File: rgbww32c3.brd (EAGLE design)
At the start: 36.8 x 20.3 mm, 19 parts, among them IC2 7805TV

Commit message: adjusted channel names
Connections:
- net CH1: now also SV1.8, U$1.5, U$1.6; no longer SV1.4, U$3.5, U$3.6
- net CH2: now also SV1.7, U$1.7, U$1.8; no longer SV1.5, U$2.7, U$2.8
- net CH4: now also SV1.5, U$2.7, U$2.8; no longer SV1.7, U$1.7, U$1.8
- net CH5: now also SV1.4, U$3.5, U$3.6; no longer SV1.8, U$1.5, U$1.6
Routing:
- net CH5: track 6.55 -> 8.59 mm
- net CH1: track 8.59 -> 6.55 mm
- net RX: track 23.8 -> 25.3 mm
- net CH4: track 7.08 -> 7.61 mm
- net CH2: track 7.61 -> 7.08 mm
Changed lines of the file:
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@@
 <text x="31.115" y="76.2" size="0.6096" layer="25">12V</text>
 <text x="31.115" y="73.66" size="0.6096" layer="25">12V</text>
-<text x="31.115" y="71.12" size="0.6096" layer="25">CH1</text>
-<text x="31.115" y="68.58" size="0.6096" layer="25">CH2</text>
+<text x="31.115" y="60.96" size="0.6096" layer="25">CH1</text>
+<text x="31.115" y="63.5" size="0.6096" layer="25">CH2</text>
 <text x="31.115" y="66.04" size="0.6096" layer="25">CH3</text>
-<text x="31.115" y="63.5" size="0.6096" layer="25">CH4</text>
-<text x="31.115" y="60.96" size="0.6096" layer="25">CH5</text>
+<text x="31.115" y="68.58" size="0.6096" layer="25">CH4</text>
+<text x="31.115" y="71.12" size="0.6096" layer="25">CH5</text>
 <wire x1="0.01" y1="80.01" x2="36.83" y2="80.01" width="0" layer="20"/>
 <text x="15.5575" y="64.92875" size="0.6096" layer="26" rot="MR90">G0</text>
@@
 </signal>
 <signal name="CH1">
-<contactref element="U$3" pad="5"/>
-<contactref element="U$3" pad="6"/>
-<contactref element="SV1" pad="4"/>
-<wire x1="34.29" y1="71.12" x2="33.02" y2="71.12" width="1.016" layer="1"/>
-<wire x1="33.02" y1="71.12" x2="29.21" y2="74.93" width="1.016" layer="1"/>
-<wire x1="29.21" y1="74.93" x2="29.21" y2="74.355" width="1.016" layer="1"/>
-<wire x1="29.21" y1="74.355" x2="29.27" y2="74.295" width="1.016" layer="1"/>
-<wire x1="29.27" y1="74.295" x2="29.27" y2="75.565" width="1.016" layer="1"/>
+<contactref element="U$1" pad="5"/>
+<contactref element="U$1" pad="6"/>
+<contactref element="SV1" pad="8"/>
+<wire x1="34.29" y1="60.96" x2="29.905" y2="60.96" width="1.016" layer="1"/>
+<wire x1="29.905" y1="60.96" x2="29.27" y2="61.595" width="1.016" layer="1"/>
+<wire x1="29.27" y1="61.595" x2="29.27" y2="62.865" width="1.016" layer="1"/>
 </signal>
 <signal name="CH3">
@@
 </signal>
 <signal name="CH2">
-<contactref element="U$2" pad="7"/>
-<contactref element="U$2" pad="8"/>
-<contactref element="SV1" pad="5"/>
-<wire x1="34.29" y1="68.58" x2="33.02" y2="68.58" width="1.016" layer="1"/>
-<wire x1="33.02" y1="68.58" x2="30.48" y2="71.12" width="1.016" layer="1"/>
-<wire x1="30.48" y1="71.12" x2="29.905" y2="71.12" width="1.016" layer="1"/>
-<wire x1="29.905" y1="71.12" x2="29.27" y2="70.485" width="1.016" layer="1"/>
-<wire x1="29.27" y1="70.485" x2="29.27" y2="71.755" width="1.016" layer="1"/>
-</signal>
-<signal name="CH4">
 <contactref element="U$1" pad="7"/>
 <contactref element="U$1" pad="8"/>
@@
 <wire x1="8.255" y1="72.54875" x2="8.09625" y2="72.39" width="0.3048" layer="1"/>
 <wire x1="8.09625" y1="72.39" x2="7.46125" y2="72.39" width="0.3048" layer="1"/>
-</signal>
-<signal name="CH5">
-<contactref element="U$1" pad="5"/>
-<contactref element="U$1" pad="6"/>
-<contactref element="SV1" pad="8"/>
-<wire x1="34.29" y1="60.96" x2="29.905" y2="60.96" width="1.016" layer="1"/>
-<wire x1="29.905" y1="60.96" x2="29.27" y2="61.595" width="1.016" layer="1"/>
-<wire x1="29.27" y1="61.595" x2="29.27" y2="62.865" width="1.016" layer="1"/>
 </signal>
 <signal name="12V">
@@
 <wire x1="13.17625" y1="72.39" x2="16.51" y2="72.39" width="0.3048" layer="1"/>
 <wire x1="16.51" y1="72.39" x2="17.145" y2="71.755" width="0.3048" layer="1"/>
-<wire x1="16.51" y1="72.39" x2="15.71625" y2="71.78875" width="0" layer="19" extent="1-16"/>
+<wire x1="15.71625" y1="71.78875" x2="17.145" y2="71.78875" width="0.3048" layer="16"/>
+<wire x1="17.145" y1="71.78875" x2="17.145" y2="71.755" width="0.3048" layer="16"/>
 </signal>
 <signal name="GPIO0">
@@
 <wire x1="16.1925" y1="68.705" x2="15.71625" y2="68.22875" width="0.3048" layer="16"/>
 </signal>
+<signal name="CH5">
+<contactref element="U$3" pad="5"/>
+<contactref element="U$3" pad="6"/>
+<contactref element="SV1" pad="4"/>
+<wire x1="34.29" y1="71.12" x2="33.02" y2="71.12" width="1.016" layer="1"/>
+<wire x1="33.02" y1="71.12" x2="29.21" y2="74.93" width="1.016" layer="1"/>
+<wire x1="29.21" y1="74.93" x2="29.21" y2="74.355" width="1.016" layer="1"/>
+<wire x1="29.21" y1="74.355" x2="29.27" y2="74.295" width="1.016" layer="1"/>
+<wire x1="29.27" y1="74.295" x2="29.27" y2="75.565" width="1.016" layer="1"/>
+</signal>
+<signal name="CH4">
+<contactref element="U$2" pad="7"/>
+<contactref element="U$2" pad="8"/>
+<contactref element="SV1" pad="5"/>
+<wire x1="34.29" y1="68.58" x2="33.02" y2="68.58" width="1.016" layer="1"/>
+<wire x1="33.02" y1="68.58" x2="30.48" y2="71.12" width="1.016" layer="1"/>
+<wire x1="30.48" y1="71.12" x2="29.905" y2="71.12" width="1.016" layer="1"/>
+<wire x1="29.905" y1="71.12" x2="29.27" y2="70.485" width="1.016" layer="1"/>
+<wire x1="29.27" y1="70.485" x2="29.27" y2="71.755" width="1.016" layer="1"/>
+</signal>
 </signals>

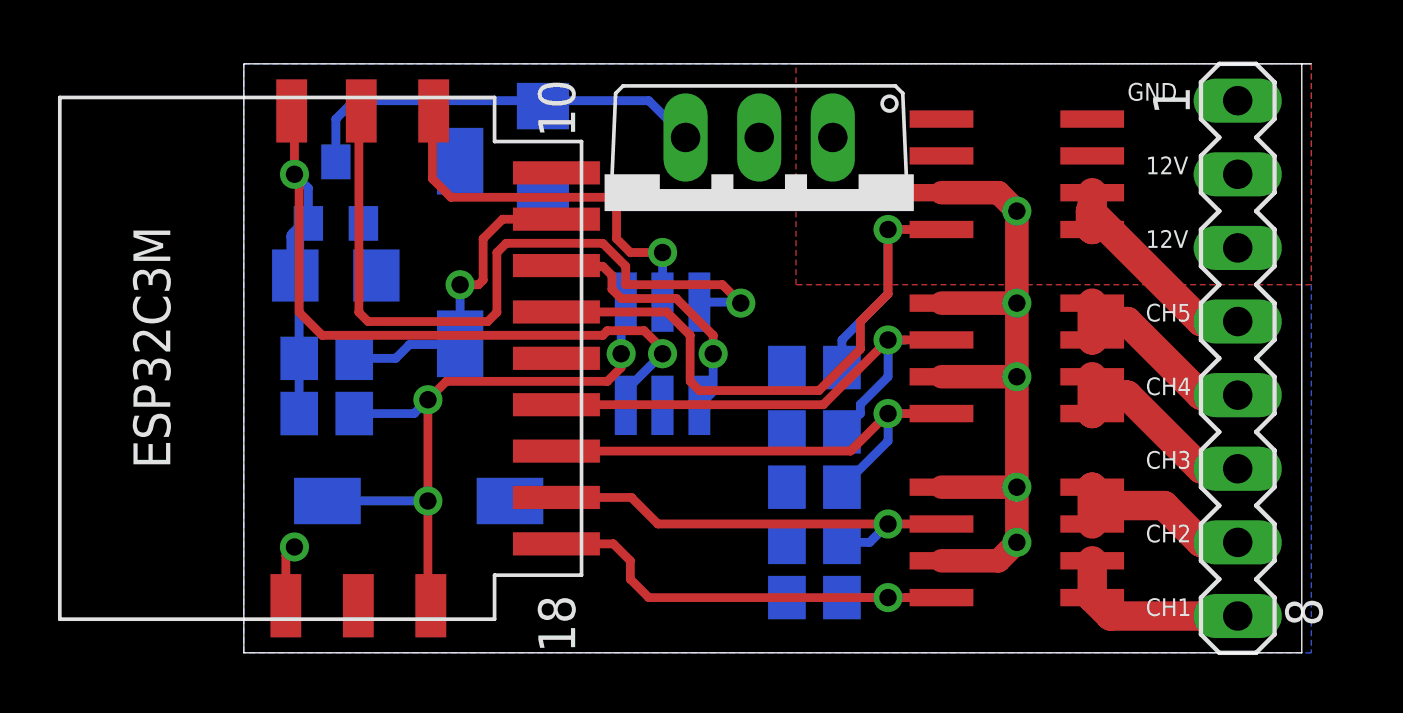
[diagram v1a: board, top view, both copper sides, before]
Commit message: initial testing version
programming the ESP32 now works using an esp_prog. It does require to pull GPIO9 low, hence the extra PRG button. The auto programming function of other ESP models (GPIO0) does not work on the C3, it seems.
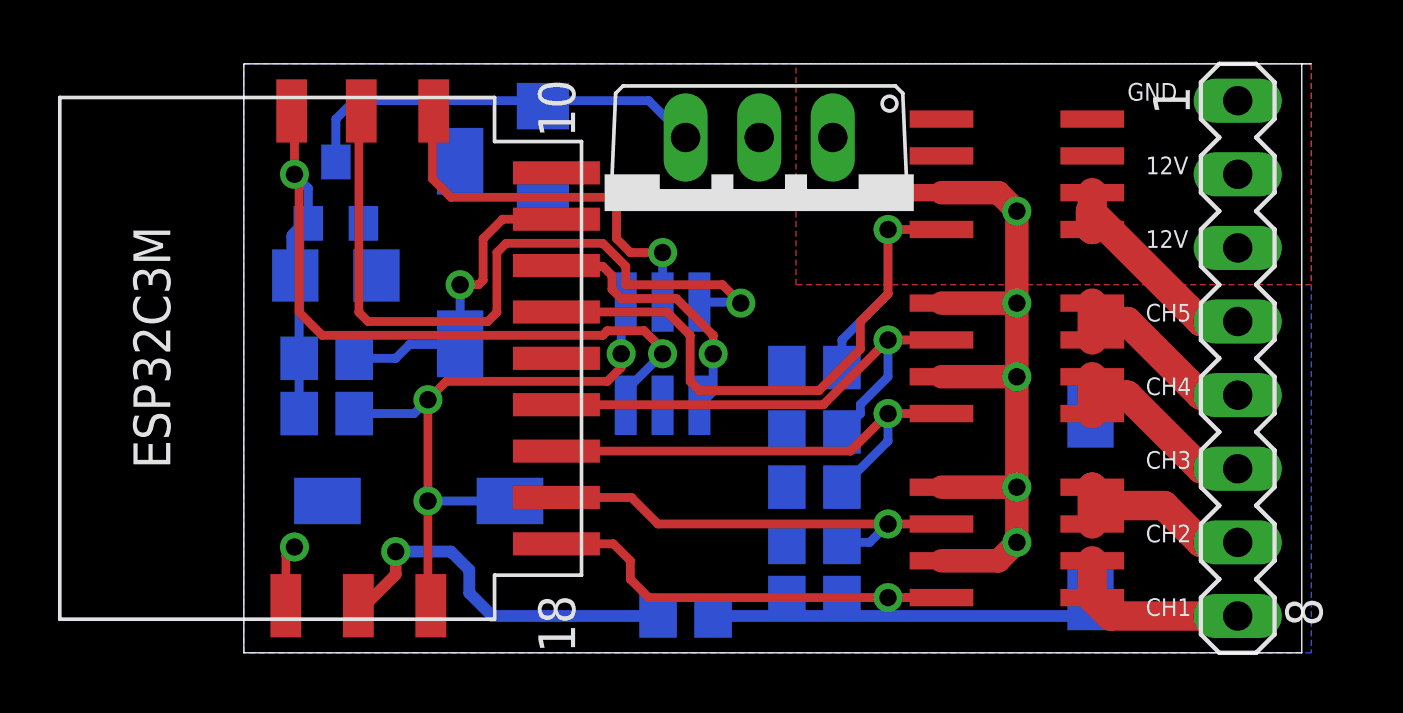
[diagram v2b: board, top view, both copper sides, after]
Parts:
- added J_PRG: 1296-T06, con-leotronics:06
- added R7: 10k, rcl:R0805
- PRG: value 1296-T06 -> (none); device con-leotronics:06 -> SparkFun-Electromechanical:TACTILE-SWITCH-1101NE
- moved PRG 15.7 mm to (29.2, 64.8), turned to 270 degrees
- turned RST to 180 degrees
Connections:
- new net N$1: R7.2, U$5.IO9
- new net N$2: PRG.2, R7.1
- net 3V3: now also J_PRG.2; no longer PRG.2
- net EN: now also J_PRG.1; no longer PRG.1
- net GND: now also J_PRG.4, PRG.1; no longer PRG.4
- net GPIO0: now also J_PRG.6; no longer PRG.6
- net RX: now also J_PRG.5; no longer PRG.5
- net TX: now also J_PRG.3; no longer PRG.3
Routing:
- net N$2: track 0.00 -> 13.3 mm
- net N$1: track 0.00 -> 13.0 mm, vias 0 -> 1
- net CH4: track 7.61 -> 6.71 mm
- net EN: track 23.0 -> 22.3 mm
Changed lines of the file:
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@@
 </element>
 <element name="R10" library="rcl" package="R0805" value="10k" x="2.8575" y="69.85" smashed="yes" rot="MR180"/>
-<element name="RST" library="SparkFun-Electromechanical" package="TACTILE-SWITCH-1101NE" value="" x="6.0325" y="64.92875" rot="MR0">
-<attribute name="PROD_ID" value="SWCH-00815" x="6.0325" y="71.27875" size="1.778" layer="28" rot="MR0" display="off"/>
+<element name="RST" library="SparkFun-Electromechanical" package="TACTILE-SWITCH-1101NE" value="" x="6.0325" y="64.92875" rot="MR180">
+<attribute name="PROD_ID" value="SWCH-00815" x="6.0325" y="58.57875" size="1.778" layer="28" rot="MR180" display="off"/>
 </element>
 <element name="R6" library="rcl" package="R0805" value="10k" x="2.8575" y="67.945" smashed="yes" rot="MR180">
 <attribute name="NAME" x="2.2225" y="66.675" size="1.27" layer="26" rot="MR180"/>
 </element>
-<element name="PRG" library="con-leotronics" package="06" value="1296-T06" x="14.44625" y="70.00875" smashed="yes" rot="MR180">
+<element name="J_PRG" library="con-leotronics" package="06" value="1296-T06" x="14.44625" y="70.00875" smashed="yes" rot="MR180">
 <attribute name="NAME" x="11.90625" y="71.27875" size="1.27" layer="26" rot="MR270"/>
 </element>
@@
 </element>
 <element name="C2" library="rcl" package="C1206" value="" x="10.31875" y="77.1525" rot="MR270"/>
+<element name="R7" library="rcl" package="R0805" value="10k" x="15.24" y="60.96" rot="MR0"/>
+<element name="PRG" library="SparkFun-Electromechanical" package="TACTILE-SWITCH-1101NE" value="" x="29.21" y="64.77" rot="MR270">
+<attribute name="PROD_ID" value="SWCH-00815" x="29.21" y="64.77" size="1.778" layer="28" rot="MR270" display="off"/>
+</element>
 </elements>
 <signals>
@@
 <contactref element="RST" pad="1"/>
 <contactref element="SV1" pad="1"/>
-<contactref element="PRG" pad="4"/>
+<contactref element="J_PRG" pad="4"/>
 <contactref element="C1" pad="2"/>
 <contactref element="C2" pad="2"/>
+<contactref element="PRG" pad="1"/>
 </signal>
 <signal name="CH1">
@@
 <contactref element="R6" pad="1"/>
 <contactref element="R10" pad="1"/>
-<contactref element="PRG" pad="2"/>
+<contactref element="J_PRG" pad="2"/>
 <contactref element="C1" pad="1"/>
 <wire x1="2.225" y1="74.505" x2="2.225" y2="75.72125" width="0.3048" layer="16"/>
@@
 <contactref element="U$5" pad="EN"/>
 <via x="6.35" y="64.92875" extent="1-16" drill="0.6"/>
-<contactref element="PRG" pad="1"/>
-<wire x1="2.8825" y1="64.92875" x2="6.35" y2="64.92875" width="0.3048" layer="16"/>
+<contactref element="J_PRG" pad="1"/>
+<wire x1="9.1825" y1="64.92875" x2="6.35" y2="64.92875" width="0.3048" layer="16"/>
 <via x="13.0175" y="70.00875" extent="1-16" drill="0.6"/>
 <wire x1="12.54125" y1="69.05625" x2="6.985" y2="69.05625" width="0.3048" layer="1"/>
@@
 </signal>
 <signal name="TX">
-<contactref element="PRG" pad="3"/>
+<contactref element="J_PRG" pad="3"/>
 <contactref element="U$5" pad="TX"/>
 <wire x1="6.55" y1="78.385" x2="6.55" y2="78.305" width="0.3048" layer="1"/>
@@
 </signal>
 <signal name="RX">
-<contactref element="PRG" pad="5"/>
+<contactref element="J_PRG" pad="5"/>
 <contactref element="U$5" pad="RX"/>
 <via x="17.145" y="71.755" extent="1-16" drill="0.6"/>
@@
 </signal>
 <signal name="GPIO0">
-<contactref element="PRG" pad="6"/>
+<contactref element="J_PRG" pad="6"/>
 <contactref element="U$5" pad="GP0"/>
 <via x="16.1925" y="70.00875" extent="1-16" drill="0.6"/>
@@
 <wire x1="33.02" y1="68.58" x2="30.48" y2="71.12" width="1.016" layer="1"/>
 <wire x1="30.48" y1="71.12" x2="29.905" y2="71.12" width="1.016" layer="1"/>
-<wire x1="29.905" y1="71.12" x2="29.27" y2="70.485" width="1.016" layer="1"/>
 <wire x1="29.27" y1="70.485" x2="29.27" y2="71.755" width="1.016" layer="1"/>
+<wire x1="29.27" y1="71.755" x2="29.905" y2="71.12" width="0" layer="19" extent="1-1"/>
+</signal>
+<signal name="N$1">
+<contactref element="U$5" pad="IO9"/>
+<contactref element="R7" pad="2"/>
+<via x="5.23875" y="63.1825" extent="1-16" drill="0.6"/>
+<wire x1="5.23875" y1="63.1825" x2="7.14375" y2="63.1825" width="0.4064" layer="16"/>
+<wire x1="7.14375" y1="63.1825" x2="7.77875" y2="62.5475" width="0.4064" layer="16"/>
+<wire x1="7.77875" y1="62.5475" x2="7.77875" y2="61.75375" width="0.4064" layer="16"/>
+<wire x1="7.77875" y1="61.75375" x2="8.5725" y2="60.96" width="0.4064" layer="16"/>
+<wire x1="8.5725" y1="60.96" x2="14.29" y2="60.96" width="0.4064" layer="16"/>
+<wire x1="3.95" y1="61.315" x2="4.165" y2="61.315" width="0.4064" layer="1"/>
+<wire x1="4.165" y1="61.315" x2="5.23875" y2="62.38875" width="0.4064" layer="1"/>
+<wire x1="5.23875" y1="62.38875" x2="5.23875" y2="63.1825" width="0.4064" layer="1"/>
+</signal>
+<signal name="N$2">
+<contactref element="PRG" pad="2"/>
+<contactref element="R7" pad="1"/>
+<wire x1="16.19" y1="60.96" x2="28.55" y2="60.96" width="0.4064" layer="16"/>
+<wire x1="28.55" y1="60.96" x2="29.21" y2="61.62" width="0.4064" layer="16"/>
 </signal>
 </signals>

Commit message: had the 12V->5V converter backwards
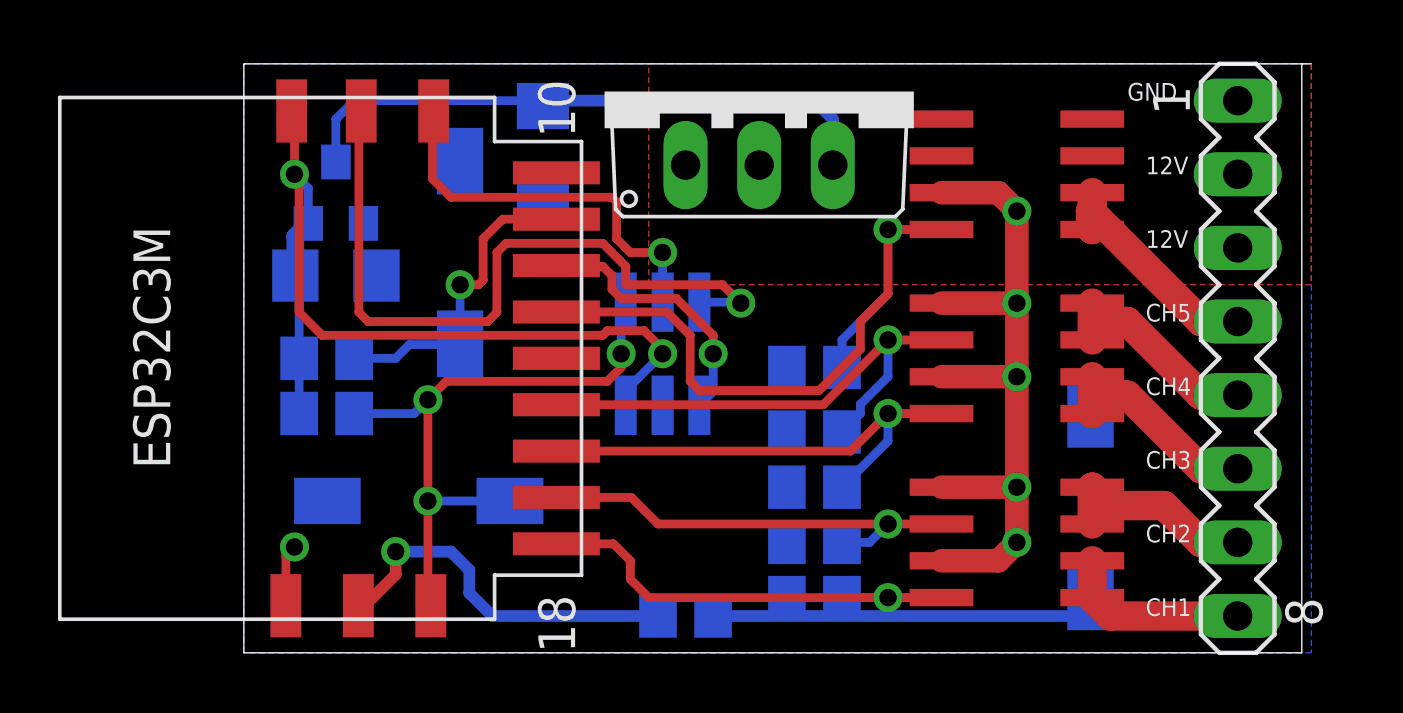
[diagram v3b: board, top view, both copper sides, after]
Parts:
- moved IC2 4.13 mm to (17.8, 79.1), turned to 0 degrees
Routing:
- net 5V: track 14.6 -> 21.0 mm
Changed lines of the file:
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@@
 </autorouter>
 <elements>
-<element name="IC2" library="linear" package="TO220V" value="7805TV" x="17.78" y="74.93" smashed="yes" rot="R180"/>
+<element name="IC2" library="linear" package="TO220V" value="7805TV" x="17.78" y="79.0575" smashed="yes"/>
 <element name="R1" library="rcl" package="R0805" value="10k" x="19.685" y="69.5325" smashed="yes" rot="MR180"/>
 <element name="R2" library="rcl" package="R0805" value="10k" x="19.685" y="65.405" smashed="yes" rot="MR0"/>
 <element name="R3" library="rcl" package="R0805" value="10k" x="19.685" y="63.5" smashed="yes" rot="MR0"/>
 <element name="R4" library="rcl" package="R0805" value="10k" x="19.685" y="61.595" smashed="yes" rot="MR0">
-<attribute name="VALUE" x="20.32" y="59.055" size="1.27" layer="28" rot="MR0"/>
+<attribute name="VALUE" x="21.59" y="70.485" size="1.27" layer="28" rot="MR0"/>
 </element>
 <element name="R5" library="rcl" package="R0805" value="10k" x="19.685" y="67.31" smashed="yes" rot="MR0"/>
@@
 </element>
 <element name="C2" library="rcl" package="C1206" value="" x="10.31875" y="77.1525" rot="MR270"/>
-<element name="R7" library="rcl" package="R0805" value="10k" x="15.24" y="60.96" rot="MR0"/>
+<element name="R7" library="rcl" package="R0805" value="10k" x="15.24" y="60.96" smashed="yes" rot="MR0">
+<attribute name="VALUE" x="15.875" y="62.23" size="1.27" layer="28" rot="MR0"/>
+</element>
 <element name="PRG" library="SparkFun-Electromechanical" package="TACTILE-SWITCH-1101NE" value="" x="29.21" y="64.77" rot="MR270">
 <attribute name="PROD_ID" value="SWCH-00815" x="29.21" y="64.77" size="1.778" layer="28" rot="MR270" display="off"/>
@@
 <contactref element="SV1" pad="2"/>
 <polygon width="0.3048" layer="1">
-<vertex x="19.05" y="80.01"/>
+<vertex x="13.97" y="80.01"/>
 <vertex x="36.83" y="80.01"/>
 <vertex x="36.83" y="72.39"/>
-<vertex x="19.05" y="72.39"/>
+<vertex x="13.97" y="72.39"/>
 </polygon>
 </signal>
@@
 <wire x1="3.81" y1="78.74" x2="3.175" y2="78.105" width="0.3048" layer="16"/>
 <wire x1="3.175" y1="78.105" x2="3.175" y2="76.625" width="0.3048" layer="16"/>
-<wire x1="13.97" y1="78.74" x2="15.24" y2="77.47" width="0.3048" layer="16"/>
 <contactref element="C2" pad="1"/>
-<wire x1="13.97" y1="78.74" x2="10.50625" y2="78.74" width="0.3048" layer="16"/>
 <wire x1="10.50625" y1="78.74" x2="10.31875" y2="78.5525" width="0.3048" layer="16"/>
+<wire x1="10.50625" y1="78.74" x2="19.685" y2="78.74" width="0.4064" layer="16"/>
+<wire x1="19.685" y1="78.74" x2="20.32" y2="78.105" width="0.4064" layer="16"/>
+<wire x1="20.32" y1="78.105" x2="20.32" y2="76.5175" width="0.4064" layer="16"/>
 </signal>
 <signal name="3V3">

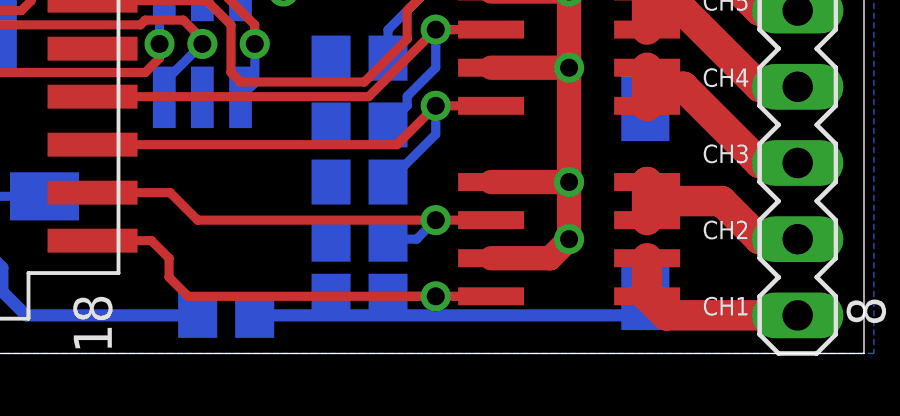
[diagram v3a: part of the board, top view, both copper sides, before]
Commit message: minor routing error
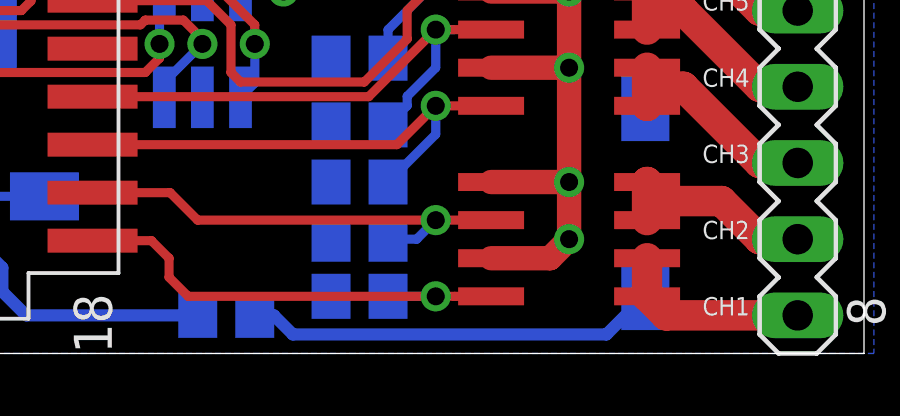
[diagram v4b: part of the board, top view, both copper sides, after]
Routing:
- net N$2: track 13.3 -> 13.8 mm
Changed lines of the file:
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@@
 <contactref element="PRG" pad="2"/>
 <contactref element="R7" pad="1"/>
-<wire x1="16.19" y1="60.96" x2="28.55" y2="60.96" width="0.4064" layer="16"/>
-<wire x1="28.55" y1="60.96" x2="29.21" y2="61.62" width="0.4064" layer="16"/>
+<wire x1="27.915" y1="60.325" x2="29.21" y2="61.62" width="0.4064" layer="16"/>
+<wire x1="16.19" y1="60.96" x2="16.8275" y2="60.96" width="0.4064" layer="16"/>
+<wire x1="16.8275" y1="60.96" x2="17.4625" y2="60.325" width="0.4064" layer="16"/>
+<wire x1="17.4625" y1="60.325" x2="27.915" y2="60.325" width="0.4064" layer="16"/>
 </signal>
 </signals>
